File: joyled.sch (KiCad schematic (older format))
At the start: 16 parts, among them P3 GAMEPAD 2, P6 GAMEPAD 1, U1 VGA SYNC/JOY BUFFER, U7 BACKLIGHT COVER

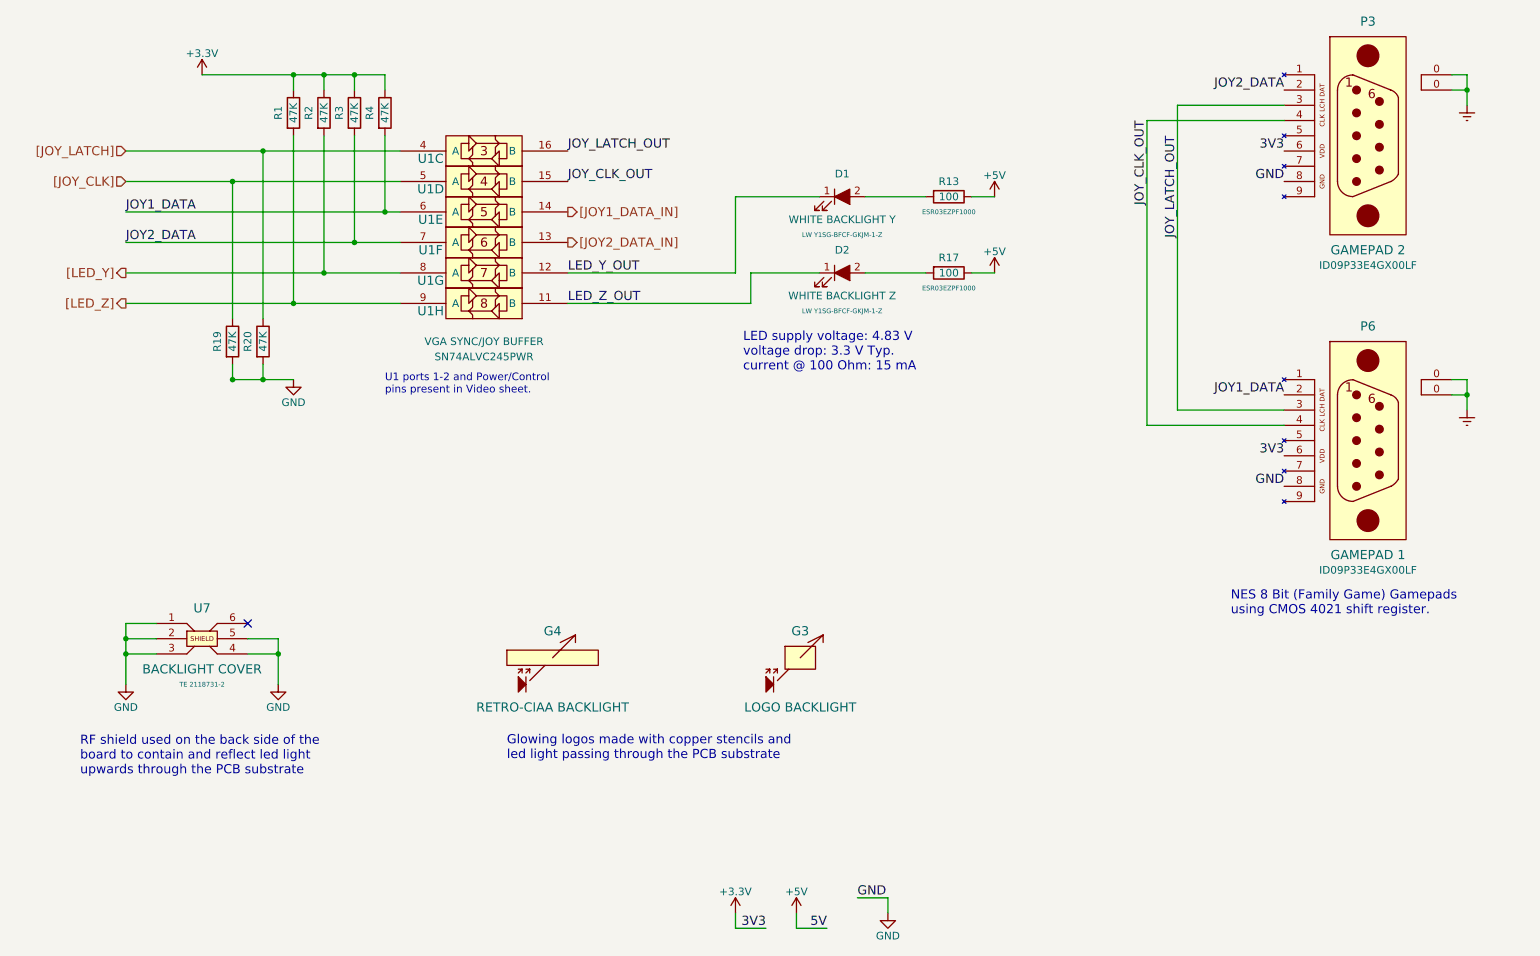
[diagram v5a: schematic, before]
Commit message: Se agrego indice en pagina 1. Union de islas de componentes con cables
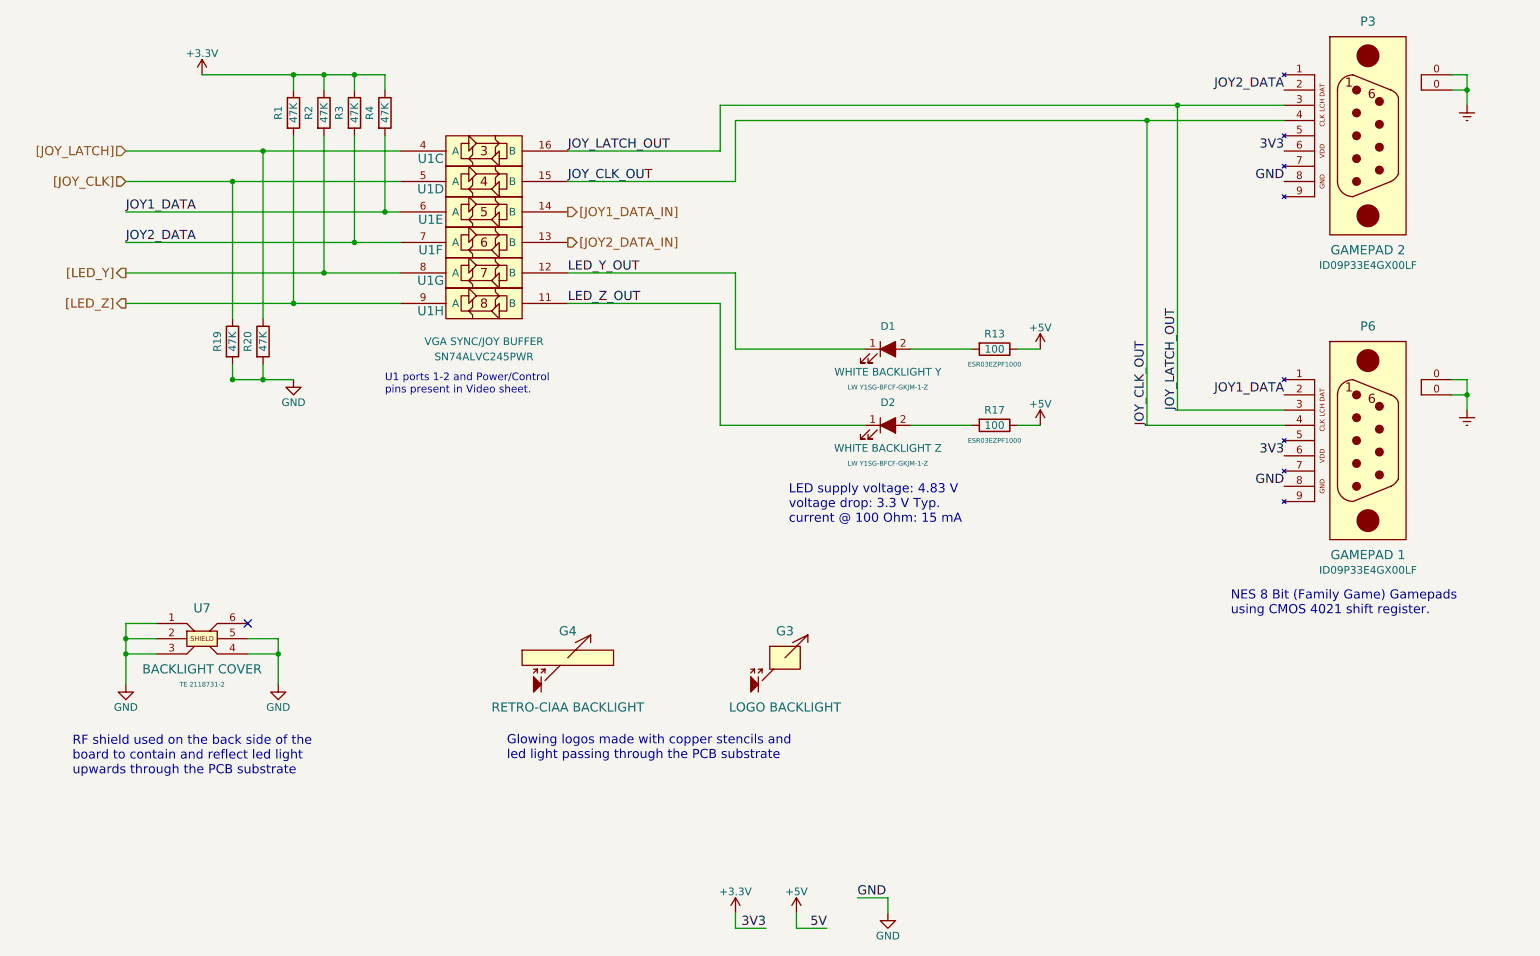
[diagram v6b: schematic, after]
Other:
- moved on the sheet: D1, D2, G3, G4, R13, R17
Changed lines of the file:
@@
 Sheet 3 8
 Title "JOYSTICKS & BACKLIGHT"
-Date "2018-10-20"
-Rev "1.1.1"
+Date "2018-11-21"
+Rev "1.2.1"
 Comp "http://www.retro-ciaa.com"
 Comment1 "All resistors 1% & 0603\" unless otherwise noted"
@@
 L LED_ALT D1
 U 1 1 5BD0B1EA
-P 6400 2700
-F 0 "D1" H 6400 2850 50  0000 C CNN
-F 1 "WHITE BACKLIGHT Y" H 6400 2550 50  0000 C CNN
-F 2 "Salmon:LED_LW_Y1SG" H 6400 2700 50  0001 C CNN
-F 3 "LW Y1SG-BFCF-GKJM-1-Z" H 6400 2450 31  0000 C CNN
-	1    6400 2700
+P 6700 3700
+F 0 "D1" H 6700 3850 50  0000 C CNN
+F 1 "WHITE BACKLIGHT Y" H 6700 3550 50  0000 C CNN
+F 2 "Salmon:LED_LW_Y1SG" H 6700 3700 50  0001 C CNN
+F 3 "LW Y1SG-BFCF-GKJM-1-Z" H 6700 3450 31  0000 C CNN
+	1    6700 3700
 	1    0    0    -1
 $EndComp
@@
 Connection ~ 3200 1900
 Wire Wire Line
-	6550 2700 6950 2700
-Wire Wire Line
-	7250 2700 7400 2700
-Wire Wire Line
-	5700 2700 6250 2700
+	6850 3700 7250 3700
+Wire Wire Line
+	7550 3700 7700 3700
+Wire Wire Line
+	5700 3200 5700 3700
 Wire Wire Line
 	3000 2000 3000 1900
@@
 	4600 3200 5700 3200
 Wire Wire Line
-	5700 3200 5700 2700
-Wire Wire Line
-	7250 3200 7400 3200
-Wire Wire Line
-	6550 3200 6950 3200
+	7550 4200 7700 4200
+Wire Wire Line
+	6850 4200 7250 4200
 $Comp
 L LED_ALT D2
 U 1 1 5BD0B22F
-P 6400 3200
-F 0 "D2" H 6400 3350 50  0000 C CNN
-F 1 "WHITE BACKLIGHT Z" H 6400 3050 50  0000 C CNN
-F 2 "Salmon:LED_LW_Y1SG" H 6400 3200 50  0001 C CNN
-F 3 "LW Y1SG-BFCF-GKJM-1-Z" H 6400 2950 31  0000 C CNN
-	1    6400 3200
+P 6700 4200
+F 0 "D2" H 6700 4350 50  0000 C CNN
+F 1 "WHITE BACKLIGHT Z" H 6700 4050 50  0000 C CNN
+F 2 "Salmon:LED_LW_Y1SG" H 6700 4200 50  0001 C CNN
+F 3 "LW Y1SG-BFCF-GKJM-1-Z" H 6700 3950 31  0000 C CNN
+	1    6700 4200
 	1    0    0    -1
 $EndComp
@@
 L +5V #PWR021
 U 1 1 5BD0B238
-P 7400 2700
-F 0 "#PWR021" H 7400 2550 50  0001 C CNN
-F 1 "+5V" H 7400 2840 50  0000 C CNN
-F 2 "" H 7400 2700 50  0000 C CNN
-F 3 "" H 7400 2700 50  0000 C CNN
-	1    7400 2700
+P 7700 3700
+F 0 "#PWR021" H 7700 3550 50  0001 C CNN
+F 1 "+5V" H 7700 3840 50  0000 C CNN
+F 2 "" H 7700 3700 50  0000 C CNN
+F 3 "" H 7700 3700 50  0000 C CNN
+	1    7700 3700
 	1    0    0    -1
 $EndComp
@@
 L +5V #PWR022
 U 1 1 5BD0B23E
-P 7400 3200
-F 0 "#PWR022" H 7400 3050 50  0001 C CNN
-F 1 "+5V" H 7400 3340 50  0000 C CNN
-F 2 "" H 7400 3200 50  0000 C CNN
-F 3 "" H 7400 3200 50  0000 C CNN
-	1    7400 3200
+P 7700 4200
+F 0 "#PWR022" H 7700 4050 50  0001 C CNN
+F 1 "+5V" H 7700 4340 50  0000 C CNN
+F 2 "" H 7700 4200 50  0000 C CNN
+F 3 "" H 7700 4200 50  0000 C CNN
+	1    7700 4200
 	1    0    0    -1
 $EndComp
@@
 L R R17
 U 1 1 5BD0B244
-P 7100 3200
-F 0 "R17" V 7000 3200 50  0000 C CNN
-F 1 "100" V 7100 3200 50  0000 C CNN
-F 2 "Resistors_SMD:R_0603" V 7030 3200 31  0001 C CNN
-F 3 "ESR03EZPF1000" V 7200 3200 31  0000 C CNN
-	1    7100 3200
+P 7400 4200
+F 0 "R17" V 7300 4200 50  0000 C CNN
+F 1 "100" V 7400 4200 50  0000 C CNN
+F 2 "Resistors_SMD:R_0603" V 7330 4200 31  0001 C CNN
+F 3 "ESR03EZPF1000" V 7500 4200 31  0000 C CNN
+	1    7400 4200
 	0    1    1    0
 $EndComp
@@
 L R R13
 U 1 1 5BD0B24B
-P 7100 2700
-F 0 "R13" V 7000 2700 50  0000 C CNN
-F 1 "100" V 7100 2700 50  0000 C CNN
-F 2 "Resistors_SMD:R_0603" V 7030 2700 31  0001 C CNN
-F 3 "ESR03EZPF1000" V 7200 2700 31  0000 C CNN
-	1    7100 2700
+P 7400 3700
+F 0 "R13" V 7300 3700 50  0000 C CNN
+F 1 "100" V 7400 3700 50  0000 C CNN
+F 2 "Resistors_SMD:R_0603" V 7330 3700 31  0001 C CNN
+F 3 "ESR03EZPF1000" V 7500 3700 31  0000 C CNN
+	1    7400 3700
 	0    1    1    0
 $EndComp
@@
 $EndComp
 Wire Wire Line
-	4600 3400 5800 3400
-Wire Wire Line
-	5800 3400 5800 3200
-Wire Wire Line
-	5800 3200 6250 3200
+	4600 3400 5600 3400
+Wire Wire Line
+	5600 3400 5600 4200
+Wire Wire Line
+	5600 4200 6550 4200
 NoConn ~ 2500 5500
 $Comp
 L INVADER_LOGO_BACK G3
 U 1 1 5BD0B291
-P 6125 5725
-F 0 "G3" H 6125 5900 60  0000 C CNN
-F 1 "LOGO BACKLIGHT" H 6125 5400 60  0000 C CNN
-F 2 "Salmon:TREX_LOGO_BACK" H 6125 5725 60  0001 C CNN
-F 3 "" H 6125 5725 60  0001 C CNN
-	1    6125 5725
+P 6025 5725
+F 0 "G3" H 6025 5900 60  0000 C CNN
+F 1 "LOGO BACKLIGHT" H 6025 5400 60  0000 C CNN
+F 2 "Salmon:TREX_LOGO_BACK" H 6025 5725 60  0001 C CNN
+F 3 "" H 6025 5725 60  0001 C CNN
+	1    6025 5725
 	1    0    0    -1
 $EndComp
@@
 L RETROCIAA_LOGO_BACK G4
 U 1 1 5BD0B298
-P 4500 5725
-F 0 "G4" H 4500 5900 60  0000 C CNN
-F 1 "RETRO-CIAA BACKLIGHT" H 4500 5400 60  0000 C CNN
-F 2 "Salmon:RETROCIAA_LOGO_BACK" H 4500 5725 60  0001 C CNN
-F 3 "" H 4500 5725 60  0001 C CNN
-	1    4500 5725
+P 4600 5725
+F 0 "G4" H 4600 5900 60  0000 C CNN
+F 1 "RETRO-CIAA BACKLIGHT" H 4600 5400 60  0000 C CNN
+F 2 "Salmon:RETROCIAA_LOGO_BACK" H 4600 5725 60  0001 C CNN
+F 3 "" H 4600 5725 60  0001 C CNN
+	1    4600 5725
 	1    0    0    -1
 $EndComp
@@
 Text Label 9300 4000 2    60   ~ 0
 JOY1_DATA
-Text Label 8600 2300 3    60   ~ 0
+Text Label 8600 4100 1    60   ~ 0
 JOY_LATCH_OUT
-Text Label 8400 2200 3    60   ~ 0
+Text Label 8400 4200 1    60   ~ 0
 JOY_CLK_OUT
 Text Notes 8950 5450 0    60   ~ 0
@@
 	8400 4200 8400 2200
 Wire Wire Line
-	8400 2200 9300 2200
+	5700 2200 9300 2200
 Wire Wire Line
 	9300 4100 8600 4100
@@
 	8600 4100 8600 2100
 Wire Wire Line
-	8600 2100 9300 2100
+	5600 2100 9300 2100
 Wire Wire Line
 	10400 2000 10500 2000
@@
 Wire Wire Line
 	10500 1900 10400 1900
-Text Notes 5750 3850 0    60   ~ 0
+Text Notes 6050 4850 0    60   ~ 0
 LED supply voltage: 4.83 V\nvoltage drop: 3.3 V Typ.\ncurrent @ 100 Ohm: 15 mA
 Text HLabel 1700 2400 0    60   Input ~ 0
@@
 Text HLabel 4600 3000 2    60   Output ~ 0
 [JOY2_DATA_IN]
-Text Notes 1400 6500 0    60   ~ 0
+Text Notes 1350 6500 0    60   ~ 0
 RF shield used on the back side of the\nboard to contain and reflect led light \nupwards through the PCB substrate
 Text Notes 4200 6400 0    60   ~ 0
 Glowing logos made with copper stencils and\nled light passing through the PCB substrate
+Wire Wire Line
+	4600 2600 5700 2600
+Wire Wire Line
+	5700 2600 5700 2200
+Connection ~ 8400 2200
+Wire Wire Line
+	4600 2400 5600 2400
+Wire Wire Line
+	5600 2400 5600 2100
+Connection ~ 8600 2100
+Wire Wire Line
+	5700 3700 6550 3700
 $EndSCHEMATC

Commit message: Limpieza de etiquetas de alimentacion
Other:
- moved on the sheet: G3, G4, U7
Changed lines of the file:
@@
 L TE_SHIELD_2118731-2 U7
 U 1 1 5BD0B281
-P 2200 5600
-F 0 "U7" H 2200 5800 60  0000 C CNN
-F 1 "BACKLIGHT COVER" H 2200 5400 60  0000 C CNN
-F 2 "Salmon:TE_SHIELD_2118731-2" H 2200 5600 60  0001 C CNN
-F 3 "TE 2118731-2" H 2200 5300 31  0000 C CNN
-	1    2200 5600
+P 2100 5800
+F 0 "U7" H 2100 6000 60  0000 C CNN
+F 1 "BACKLIGHT COVER" H 2100 5600 60  0000 C CNN
+F 2 "Salmon:TE_SHIELD_2118731-2" H 2100 5800 60  0001 C CNN
+F 3 "TE 2118731-2" H 2100 5500 31  0000 C CNN
+	1    2100 5800
 	1    0    0    -1
 $EndComp
@@
 Wire Wire Line
 	5600 4200 6550 4200
-NoConn ~ 2500 5500
+NoConn ~ 2400 5700
 $Comp
 L INVADER_LOGO_BACK G3
 U 1 1 5BD0B291
-P 6025 5725
-F 0 "G3" H 6025 5900 60  0000 C CNN
-F 1 "LOGO BACKLIGHT" H 6025 5400 60  0000 C CNN
-F 2 "Salmon:TREX_LOGO_BACK" H 6025 5725 60  0001 C CNN
-F 3 "" H 6025 5725 60  0001 C CNN
-	1    6025 5725
+P 5925 5925
+F 0 "G3" H 5925 6100 60  0000 C CNN
+F 1 "LOGO BACKLIGHT" H 5925 5600 60  0000 C CNN
+F 2 "Salmon:TREX_LOGO_BACK" H 5925 5925 60  0001 C CNN
+F 3 "" H 5925 5925 60  0001 C CNN
+	1    5925 5925
 	1    0    0    -1
 $EndComp
@@
 L RETROCIAA_LOGO_BACK G4
 U 1 1 5BD0B298
-P 4600 5725
-F 0 "G4" H 4600 5900 60  0000 C CNN
-F 1 "RETRO-CIAA BACKLIGHT" H 4600 5400 60  0000 C CNN
-F 2 "Salmon:RETROCIAA_LOGO_BACK" H 4600 5725 60  0001 C CNN
-F 3 "" H 4600 5725 60  0001 C CNN
-	1    4600 5725
+P 4500 5925
+F 0 "G4" H 4500 6100 60  0000 C CNN
+F 1 "RETRO-CIAA BACKLIGHT" H 4500 5600 60  0000 C CNN
+F 2 "Salmon:RETROCIAA_LOGO_BACK" H 4500 5925 60  0001 C CNN
+F 3 "" H 4500 5925 60  0001 C CNN
+	1    4500 5925
 	1    0    0    -1
 $EndComp
@@
 	1    0    0    -1
 $EndComp
-Text Label 9300 2400 2    60   ~ 0
-3V3
-Text Label 9300 4400 2    60   ~ 0
-3V3
-Text Label 9300 2600 2    60   ~ 0
-GND
-Text Label 9300 4600 2    60   ~ 0
-GND
 Text Label 9300 2000 2    60   ~ 0
 JOY2_DATA
@@
 L GND #PWR025
 U 1 1 5BD2F9D4
-P 1700 5900
-F 0 "#PWR025" H 1700 5650 50  0001 C CNN
-F 1 "GND" H 1700 5750 50  0000 C CNN
-F 2 "" H 1700 5900 50  0000 C CNN
-F 3 "" H 1700 5900 50  0000 C CNN
-	1    1700 5900
+P 1600 6100
+F 0 "#PWR025" H 1600 5850 50  0001 C CNN
+F 1 "GND" H 1600 5950 50  0000 C CNN
+F 2 "" H 1600 6100 50  0000 C CNN
+F 3 "" H 1600 6100 50  0000 C CNN
+	1    1600 6100
 	1    0    0    -1
 $EndComp
@@
 L GND #PWR026
 U 1 1 5BD2FA3A
-P 2700 5900
-F 0 "#PWR026" H 2700 5650 50  0001 C CNN
-F 1 "GND" H 2700 5750 50  0000 C CNN
-F 2 "" H 2700 5900 50  0000 C CNN
-F 3 "" H 2700 5900 50  0000 C CNN
-	1    2700 5900
-	1    0    0    -1
-$EndComp
-Wire Wire Line
-	1900 5500 1700 5500
-Wire Wire Line
-	1700 5500 1700 5900
-Wire Wire Line
-	1900 5600 1700 5600
-Connection ~ 1700 5600
-Wire Wire Line
-	1900 5700 1700 5700
-Connection ~ 1700 5700
-Wire Wire Line
-	2500 5600 2700 5600
-Wire Wire Line
-	2700 5600 2700 5900
-Wire Wire Line
-	2500 5700 2700 5700
-Connection ~ 2700 5700
-Text Label 6300 7500 2    60   ~ 0
-5V
-Text Label 5900 7500 2    60   ~ 0
-3V3
-$Comp
-L +5V #PWR027
-U 1 1 5BD5D879
-P 6100 7400
-F 0 "#PWR027" H 6100 7250 50  0001 C CNN
-F 1 "+5V" H 6100 7540 50  0000 C CNN
-F 2 "" H 6100 7400 50  0000 C CNN
-F 3 "" H 6100 7400 50  0000 C CNN
-	1    6100 7400
-	1    0    0    -1
-$EndComp
-$Comp
-L +3.3V #PWR028
-U 1 1 5BD5D87F
-P 5700 7400
-F 0 "#PWR028" H 5700 7250 50  0001 C CNN
-F 1 "+3.3V" H 5700 7540 50  0000 C CNN
-F 2 "" H 5700 7400 50  0000 C CNN
-F 3 "" H 5700 7400 50  0000 C CNN
-	1    5700 7400
-	1    0    0    -1
-$EndComp
-$Comp
-L GND #PWR029
-U 1 1 5BD5D885
-P 6700 7400
-F 0 "#PWR029" H 6700 7150 50  0001 C CNN
-F 1 "GND" H 6700 7250 50  0000 C CNN
-F 2 "" H 6700 7400 50  0000 C CNN
-F 3 "" H 6700 7400 50  0000 C CNN
-	1    6700 7400
-	1    0    0    -1
-$EndComp
-Text Label 6500 7300 0    60   ~ 0
-GND
-Wire Wire Line
-	5700 7400 5700 7500
-Wire Wire Line
-	5700 7500 5900 7500
-Wire Wire Line
-	6100 7400 6100 7500
-Wire Wire Line
-	6100 7500 6300 7500
-Wire Wire Line
-	6500 7300 6700 7300
-Wire Wire Line
-	6700 7300 6700 7400
+P 2600 6100
+F 0 "#PWR026" H 2600 5850 50  0001 C CNN
+F 1 "GND" H 2600 5950 50  0000 C CNN
+F 2 "" H 2600 6100 50  0000 C CNN
+F 3 "" H 2600 6100 50  0000 C CNN
+	1    2600 6100
+	1    0    0    -1
+$EndComp
+Wire Wire Line
+	1800 5700 1600 5700
+Wire Wire Line
+	1600 5700 1600 6100
+Wire Wire Line
+	1800 5800 1600 5800
+Connection ~ 1600 5800
+Wire Wire Line
+	1800 5900 1600 5900
+Connection ~ 1600 5900
+Wire Wire Line
+	2400 5800 2600 5800
+Wire Wire Line
+	2600 5800 2600 6100
+Wire Wire Line
+	2400 5900 2600 5900
+Connection ~ 2600 5900
 Text Label 1700 3000 0    60   ~ 0
 JOY2_DATA
@@
 Text HLabel 4600 3000 2    60   Output ~ 0
 [JOY2_DATA_IN]
-Text Notes 1350 6500 0    60   ~ 0
+Text Notes 1250 6700 0    60   ~ 0
 RF shield used on the back side of the\nboard to contain and reflect led light \nupwards through the PCB substrate
-Text Notes 4200 6400 0    60   ~ 0
+Text Notes 4100 6600 0    60   ~ 0
 Glowing logos made with copper stencils and\nled light passing through the PCB substrate
 Wire Wire Line
@@
 Wire Wire Line
 	5700 3700 6550 3700
+$Comp
+L GND #PWR027
+U 1 1 5BF79EA4
+P 9100 4600
+F 0 "#PWR027" H 9100 4350 50  0001 C CNN
+F 1 "GND" H 9100 4450 50  0000 C CNN
+F 2 "" H 9100 4600 50  0000 C CNN
+F 3 "" H 9100 4600 50  0000 C CNN
+	1    9100 4600
+	1    0    0    -1
+$EndComp
+$Comp
+L GND #PWR028
+U 1 1 5BF79FFF
+P 9100 2600
+F 0 "#PWR028" H 9100 2350 50  0001 C CNN
+F 1 "GND" H 9100 2450 50  0000 C CNN
+F 2 "" H 9100 2600 50  0000 C CNN
+F 3 "" H 9100 2600 50  0000 C CNN
+	1    9100 2600
+	1    0    0    -1
+$EndComp
+$Comp
+L +3.3V #PWR029
+U 1 1 5BF7A0C7
+P 9100 2400
+F 0 "#PWR029" H 9100 2250 50  0001 C CNN
+F 1 "+3.3V" H 9100 2540 50  0000 C CNN
+F 2 "" H 9100 2400 50  0000 C CNN
+F 3 "" H 9100 2400 50  0000 C CNN
+	1    9100 2400
+	1    0    0    -1
+$EndComp
+$Comp
+L +3.3V #PWR030
+U 1 1 5BF7A222
+P 9100 4400
+F 0 "#PWR030" H 9100 4250 50  0001 C CNN
+F 1 "+3.3V" H 9100 4540 50  0000 C CNN
+F 2 "" H 9100 4400 50  0000 C CNN
+F 3 "" H 9100 4400 50  0000 C CNN
+	1    9100 4400
+	1    0    0    -1
+$EndComp
+Wire Wire Line
+	9100 2400 9300 2400
+Wire Wire Line
+	9300 2600 9100 2600
+Wire Wire Line
+	9100 4400 9300 4400
+Wire Wire Line
+	9300 4600 9100 4600
 $EndSCHEMATC
